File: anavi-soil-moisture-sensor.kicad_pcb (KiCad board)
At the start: 2 copper layers, 22.9 x 61 mm, 9 parts, among them P1 CONN_01X03, P2 CONN_01X01, P3 CONN_01X01, Q1 BC817

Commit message: anavi-soil-moisture-sensor.kicad_pcb: Fix pads
Signed-off-by: Leon Anavi <leon@anavi.org>
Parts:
- moved P2 20.8 mm to (140.8, 113.3)
- moved P3 20.8 mm to (156.1, 113.3)
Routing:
- net Net-(P3-Pad1): vias 0 -> 19
- net Net-(P2-Pad1): vias 0 -> 19
- net (no net): vias 40 -> 0
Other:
- board text added: "Rev 1.1 (c) 2017"
- board text removed: "Rev 1.0 (c) 2017"

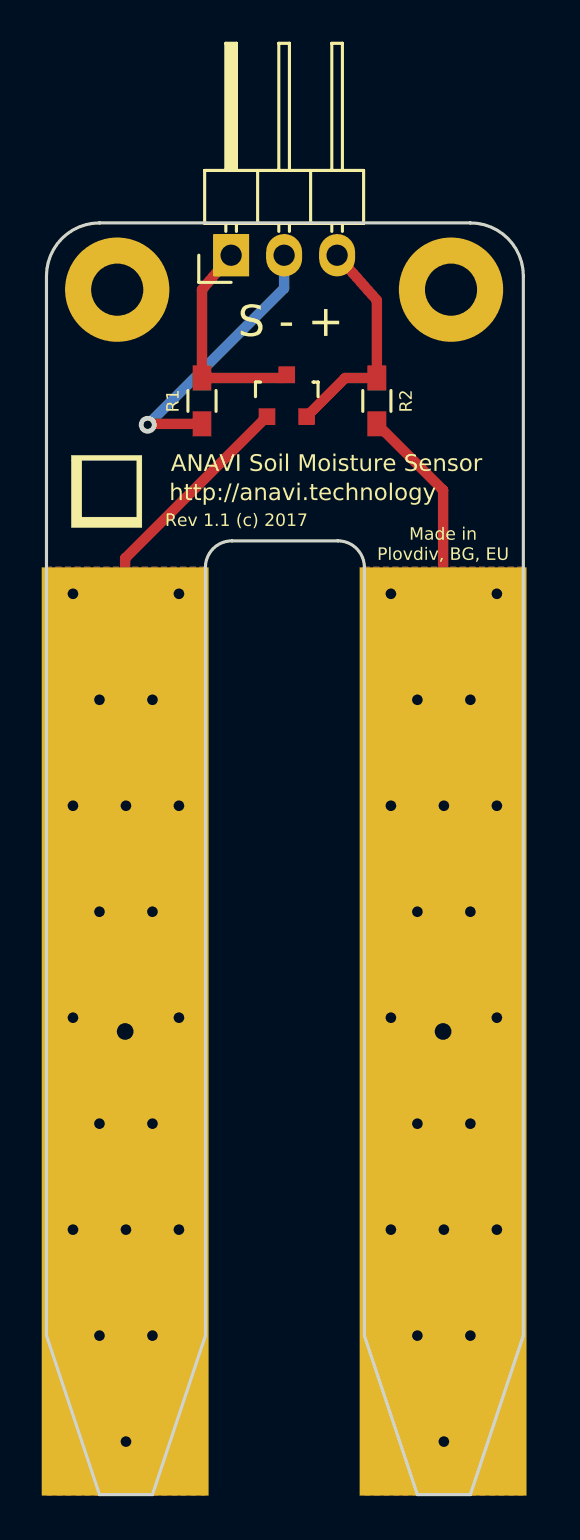
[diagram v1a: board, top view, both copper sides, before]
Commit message: anavi-soil-moisture-sensor.kicad_pcb: Add vias
Signed-off-by: Leon Anavi <leon@anavi.org>
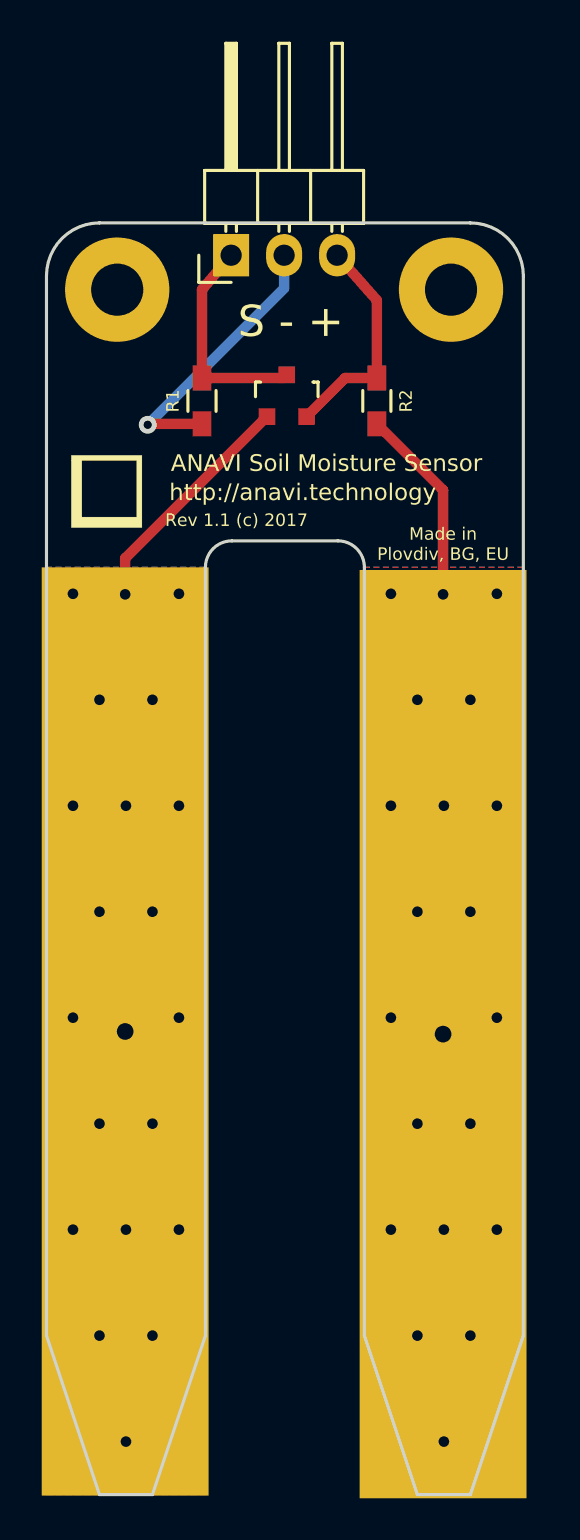
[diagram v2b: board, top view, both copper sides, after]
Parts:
- moved P3 0.13 mm to (156.1, 113.4)
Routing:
- net Net-(P3-Pad1): vias 19 -> 20
- net Net-(P2-Pad1): vias 19 -> 20
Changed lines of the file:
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@@
     (thickness 1.6)
     (drawings 45)
-    (tracks 57)
+    (tracks 59)
     (zones 0)
     (modules 9)
@@
   )
   (module Wire_Pads:SolderWirePad_single_0-8mmDrill (layer Top)
-    (at 156.083 113.284)
+    (at 156.083 113.411)
     (fp_text reference P3 (at 0 -2.54) (layer F.SilkS) hide
       (effects (font (size 1 1) (thickness 0.15)))
@@
   (segment (start 152.908 81.958) (end 151.38676 81.958) (width 0.5) (layer Top) (net 5))
   (segment (start 151.38676 81.958) (end 149.54 83.80476) (width 0.5) (layer Top) (net 5))
+  (via (at 140.8811 132.9436) (size 1.016) (drill 0.508) (layers Top Bottom) (net 6))
+  (via (at 140.843 92.329) (size 1.016) (drill 0.508) (layers Top Bottom) (net 6))
   (via (at 138.3411 122.7836) (size 1.016) (drill 0.508) (layers Top Bottom) (net 6))
   (via (at 140.8811 122.7836) (size 1.016) (drill 0.508) (layers Top Bottom) (net 6))
@@
   (via (at 142.1511 127.8636) (size 1.016) (drill 0.508) (layers Top Bottom) (net 6))
   (via (at 139.6111 127.8636) (size 1.016) (drill 0.508) (layers Top Bottom) (net 6))
-  (via (at 140.8811 132.9436) (size 1.016) (drill 0.508) (layers Top Bottom) (net 6))
   (segment (start 140.843 92.456) (end 140.843 90.60176) (width 0.5) (layer Top) (net 6))
   (segment (start 140.843 90.60176) (end 147.64 83.80476) (width 0.5) (layer Top) (net 6))
@@
   (via (at 157.3911 127.8636) (size 1.016) (drill 0.508) (layers Top Bottom) (net 7))
   (via (at 156.1211 132.9436) (size 1.016) (drill 0.508) (layers Top Bottom) (net 7))
+  (via (at 158.6611 122.7836) (size 1.016) (drill 0.508) (layers Top Bottom) (net 7))
+  (via (at 156.1211 122.7836) (size 1.016) (drill 0.508) (layers Top Bottom) (net 7))
+  (via (at 153.5811 122.7836) (size 1.016) (drill 0.508) (layers Top Bottom) (net 7))
+  (via (at 154.8511 117.7036) (size 1.016) (drill 0.508) (layers Top Bottom) (net 7))
+  (via (at 157.3911 117.7036) (size 1.016) (drill 0.508) (layers Top Bottom) (net 7))
+  (via (at 156.083 92.329) (size 1.016) (drill 0.508) (layers Top Bottom) (net 7))
   (via (at 153.5811 92.3036) (size 1.016) (drill 0.508) (layers Top Bottom) (net 7))
   (via (at 158.6611 92.3036) (size 1.016) (drill 0.508) (layers Top Bottom) (net 7))
@@
   (via (at 153.5811 112.6236) (size 1.016) (drill 0.508) (layers Top Bottom) (net 7))
   (via (at 158.6611 112.6236) (size 1.016) (drill 0.508) (layers Top Bottom) (net 7))
-  (via (at 158.6611 122.7836) (size 1.016) (drill 0.508) (layers Top Bottom) (net 7))
-  (via (at 156.1211 122.7836) (size 1.016) (drill 0.508) (layers Top Bottom) (net 7))
-  (via (at 153.5811 122.7836) (size 1.016) (drill 0.508) (layers Top Bottom) (net 7))
   (via (at 154.8511 97.3836) (size 1.016) (drill 0.508) (layers Top Bottom) (net 7))
   (via (at 157.3911 97.3836) (size 1.016) (drill 0.508) (layers Top Bottom) (net 7))
   (via (at 157.3911 107.5436) (size 1.016) (drill 0.508) (layers Top Bottom) (net 7))
   (via (at 154.8511 107.5436) (size 1.016) (drill 0.508) (layers Top Bottom) (net 7))
-  (via (at 154.8511 117.7036) (size 1.016) (drill 0.508) (layers Top Bottom) (net 7))
-  (via (at 157.3911 117.7036) (size 1.016) (drill 0.508) (layers Top Bottom) (net 7))
   (segment (start 156.083 92.456) (end 156.083 87.333) (width 0.5) (layer Top) (net 7))
   (segment (start 156.083 87.333) (end 152.908 84.158) (width 0.5) (layer Top) (net 7))

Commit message: anavi-soil-moisture-sensor.kicad_pcb: Revision 1.1
Signed-off-by: Leon Anavi <leon@anavi.org>
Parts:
- moved P3 0.13 mm to (156.1, 113.3)
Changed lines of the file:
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@@
     (links 7)
     (no_connects 0)
-    (area 136.996099 74.448599 160.006101 135.558601)
+    (area 130.493714 65.143999 166.432286 135.788)
     (thickness 1.6)
     (drawings 45)
@@
       (drillshape 0)
       (scaleselection 1)
-      (outputdirectory plots/plot-1.0/))
+      (outputdirectory plots/plot-1.1/))
   )
   (net 0 "")
@@
   )
   (module Wire_Pads:SolderWirePad_single_0-8mmDrill (layer Top)
-    (at 156.083 113.411)
+    (at 156.083 113.284)
     (fp_text reference P3 (at 0 -2.54) (layer F.SilkS) hide
       (effects (font (size 1 1) (thickness 0.15)))

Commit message: anavi-soil-moisture-sensor: Assembly guidelines
Add labels for assembly guidelines of SMT components.

Signed-off-by: Leon Anavi <leon@anavi.org>
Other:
- board text added: "BC817"
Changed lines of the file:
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@@
-(kicad_pcb (version 4) (host pcbnew 4.0.4+dfsg1-stable)
+(kicad_pcb (version 4) (host pcbnew 4.0.5+dfsg1-4)
   (general
     (links 7)
@@
     (area 130.493714 65.143999 166.432286 135.788)
     (thickness 1.6)
-    (drawings 45)
+    (drawings 46)
     (tracks 59)
     (zones 0)
@@
   (page A4)
   (layers
-    (0 Top signal)
-    (31 Bottom signal)
-    (32 B.Adhes user)
-    (33 F.Adhes user)
-    (34 B.Paste user)
-    (35 F.Paste user)
-    (36 B.SilkS user)
-    (37 F.SilkS user)
+    (0 Top signal hide)
+    (31 Bottom signal hide)
+    (32 B.Adhes user hide)
+    (33 F.Adhes user hide)
+    (34 B.Paste user hide)
+    (35 F.Paste user hide)
+    (36 B.SilkS user hide)
+    (37 F.SilkS user hide)
     (38 B.Mask user)
     (39 F.Mask user)
-    (40 Dwgs.User user)
-    (41 Cmts.User user)
-    (42 Eco1.User user)
-    (43 Eco2.User user)
+    (40 Dwgs.User user hide)
+    (41 Cmts.User user hide)
+    (42 Eco1.User user hide)
+    (43 Eco2.User user hide)
     (44 Edge.Cuts user)
     (45 Margin user)
     (46 B.CrtYd user)
     (47 F.CrtYd user)
-    (48 B.Fab user)
+    (48 B.Fab user hide)
     (49 F.Fab user)
   )
@@
     (pad_to_mask_clearance 0.2)
     (aux_axis_origin 0 0)
-    (visible_elements FFFFFF7F)
+    (visible_elements FFFF5121)
     (pcbplotparams
       (layerselection 0x010f0_80000001)
@@
       (drillshape 0)
       (scaleselection 1)
-      (outputdirectory plots/plot-1.1/))
+      (outputdirectory plots/plot-1.1/assembly.svg))
   )
   (net 0 "")
@@
       (xy -1.693333 -1.524) (xy -1.693333 -1.778) (xy 1.693334 -1.778) (xy 1.693334 1.693334)) (layer F.SilkS) (width 0.01))
   )
+  (gr_text BC817 (at 148.59 83.312) (layer F.Fab)
+    (effects (font (size 0.6 0.6) (thickness 0.15)))
+  )
   (gr_text "Made in \nPlovdiv, BG, EU" (at 156.083 89.916) (layer F.SilkS)
